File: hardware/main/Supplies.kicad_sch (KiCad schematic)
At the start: 9 parts, among them J601 Supplies, U601 VXO7805-1000, U602 AMS1117-3.3

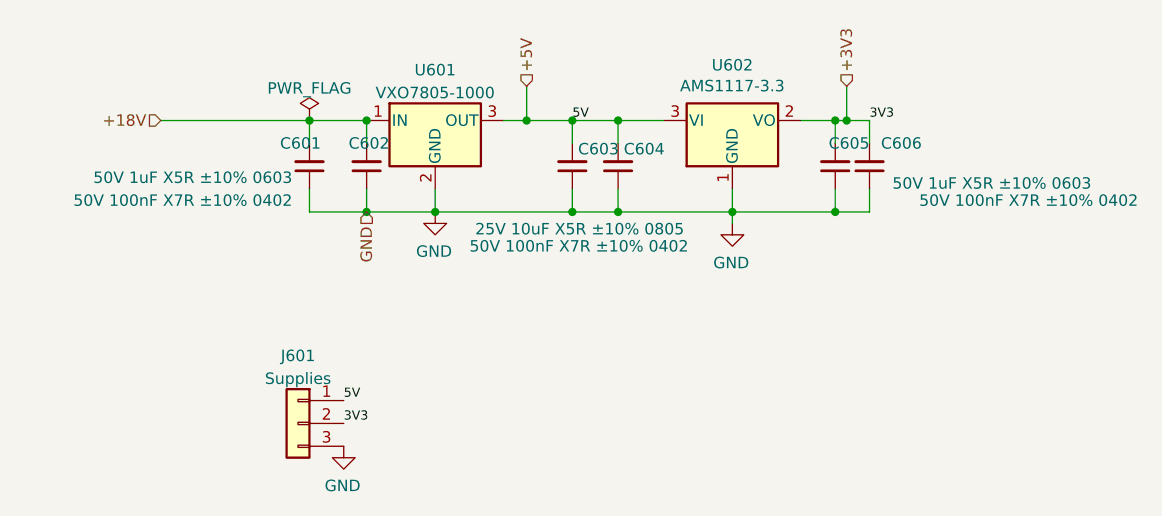
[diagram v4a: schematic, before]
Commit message: layout: Separating analogical power nets
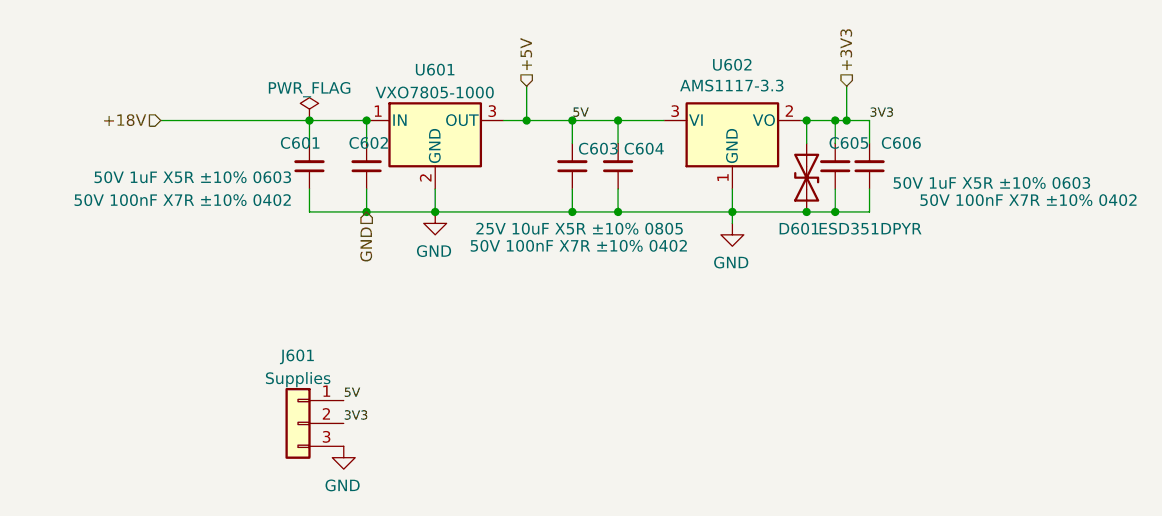
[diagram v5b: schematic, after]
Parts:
- added D601: ESD351DPYR, Diode_SMD:D_0402_1005Metric_Pad0.77x0.64mm_HandSolder, symbol Device:D_TVS
- U601: footprint Zenite:TO-220-3_Horizontal_TabDown_SMD -> Zenite:TO-220-3_Horizontal_TabDown_SMD_3
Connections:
- net +3V3: now also D601.2 (A2)
- net GND: now also D601.1 (A1)
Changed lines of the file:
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@@
   (junction (at 136.525 83.185) (diameter 0) (color 0 0 0 0)
   )
+  (junction (at 177.8 83.185) (diameter 0) (color 0 0 0 0)
+  )
   (junction (at 156.845 83.185) (diameter 0) (color 0 0 0 0)
   )
@@
   (junction (at 156.845 73.025) (diameter 0) (color 0 0 0 0)
   )
+  (junction (at 177.8 73.025) (diameter 0) (color 0 0 0 0)
+  )
   (junction (at 180.975 83.185) (diameter 0) (color 0 0 0 0)
   )
@@
     (stroke (width 0) (type default) (color 0 0 0 0))
   )
+  (wire (pts (xy 177.8 83.185) (xy 169.545 83.185))
+    (stroke (width 0) (type default) (color 0 0 0 0))
+  )
   (wire (pts (xy 128.905 73.025) (xy 122.555 73.025))
     (stroke (width 0) (type default) (color 0 0 0 0))
@@
     (stroke (width 0) (type default) (color 0 0 0 0))
   )
+  (wire (pts (xy 177.8 73.025) (xy 177.165 73.025))
+    (stroke (width 0) (type default) (color 0 0 0 0))
+  )
   (wire (pts (xy 146.685 69.215) (xy 146.685 73.025))
     (stroke (width 0) (type default) (color 0 0 0 0))
@@
     (stroke (width 0) (type default) (color 0 0 0 0))
   )
-  (wire (pts (xy 180.975 73.025) (xy 177.165 73.025))
-    (stroke (width 0) (type default) (color 0 0 0 0))
-  )
-  (wire (pts (xy 180.975 83.185) (xy 169.545 83.185))
+  (wire (pts (xy 180.975 73.025) (xy 177.8 73.025))
+    (stroke (width 0) (type default) (color 0 0 0 0))
+  )
+  (wire (pts (xy 180.975 83.185) (xy 177.8 83.185))
     (stroke (width 0) (type default) (color 0 0 0 0))
   )
@@
   )
   (wire (pts (xy 151.765 80.645) (xy 151.765 83.185))
+    (stroke (width 0) (type default) (color 0 0 0 0))
+  )
+  (wire (pts (xy 177.8 73.025) (xy 177.8 75.565))
     (stroke (width 0) (type default) (color 0 0 0 0))
   )
@@
     )
     (pin "1")
+  )
+  (symbol (lib_id "Device:D_TVS") (at 177.8 79.375 90) (unit 1)
+    (in_bom yes) (on_board yes)
+    (property "Reference" "D601" (id 0) (at 174.625 85.09 90)
+      (effects (font (size 1.27 1.27)) (justify right))
+    )
+    (property "Value" "ESD351DPYR" (id 1) (at 179.07 85.09 90)
+      (effects (font (size 1.27 1.27)) (justify right))
+    )
+    (property "Footprint" "Diode_SMD:D_0402_1005Metric_Pad0.77x0.64mm_HandSolder" (id 2) (at 177.8 79.375 0)
+      (effects (font (size 1.27 1.27)) hide)
+    )
+    (property "Datasheet" "~" (id 3) (at 177.8 79.375 0)
+      (effects (font (size 1.27 1.27)) hide)
+    )
+    (pin "1")
+    (pin "2")
   )
   (symbol (lib_id "Regulator_Linear:L7805") (at 136.525 73.025 0) (unit 1)
@@
     (property "Reference" "U601" (id 0) (at 136.525 67.4202 0))
     (property "Value" "VXO7805-1000" (id 1) (at 136.525 69.9571 0))
-    (property "Footprint" "Zenite:TO-220-3_Horizontal_TabDown_SMD" (id 2) (at 137.16 76.835 0)
+    (property "Footprint" "Zenite:TO-220-3_Horizontal_TabDown_SMD_3" (id 2) (at 137.16 76.835 0)
       (effects (font (size 1.27 1.27) italic) (justify left) hide)
     )

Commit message: Layout: Place components and route analog, supplies and CAN
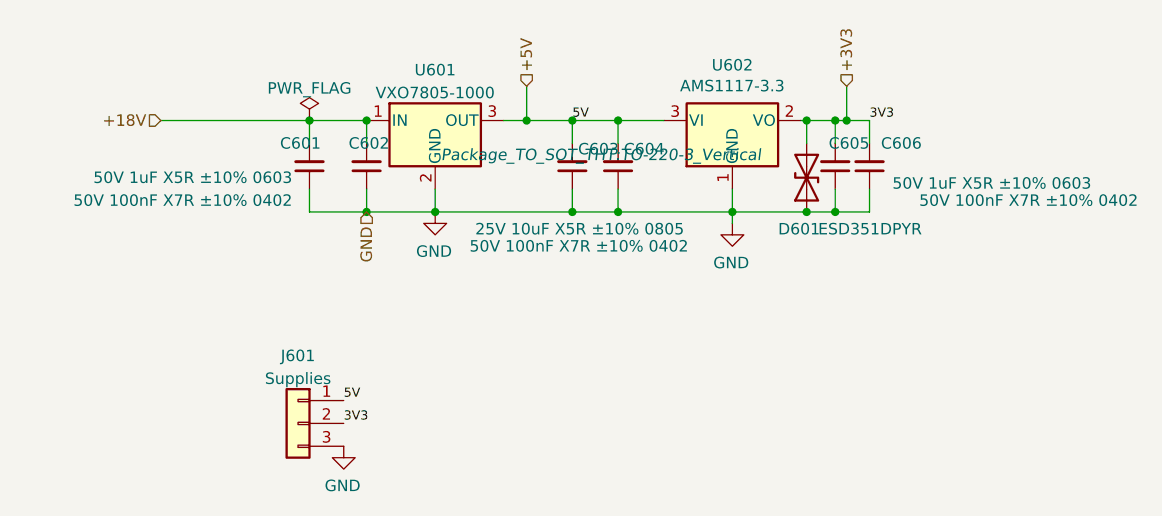
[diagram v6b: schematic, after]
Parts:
- U601: footprint Zenite:TO-220-3_Horizontal_TabDown_SMD_3 -> Package_TO_SOT_THT:TO-220-3_Vertical
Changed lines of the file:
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@@
     (property "Reference" "U601" (id 0) (at 136.525 67.4202 0))
     (property "Value" "VXO7805-1000" (id 1) (at 136.525 69.9571 0))
-    (property "Footprint" "Zenite:TO-220-3_Horizontal_TabDown_SMD_3" (id 2) (at 137.16 76.835 0)
-      (effects (font (size 1.27 1.27) italic) (justify left) hide)
+    (property "Footprint" "Package_TO_SOT_THT:TO-220-3_Vertical" (id 2) (at 137.16 76.835 0)
+      (effects (font (size 1.27 1.27) italic) (justify left))
     )
     (property "Datasheet" "https://www.mouser.com/ProductDetail/CUI-Inc/VXO7805-1000?qs=HXFqYaX1Q2zTUq5iRuYtuQ%3D%3D" (id 3) (at 136.525 74.295 0)
